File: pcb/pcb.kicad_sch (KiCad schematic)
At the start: 44 parts, among them J1 Conn_01x02_Socket, J2 Conn_01x04_Socket, U1 AP2112K-3.3TRG1, U2 W25Q16JVUXIQ, U3 RP2040, U4 DS4432U+T&amp;R, U5 AD8403ARUZ1-REEL, U6 ADG801BRTZ-REEL7, Y2 Crystal_GND24_Small

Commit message: Order ready
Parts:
- C10, C11, C12, C13, C14, C15, C16, C18, C19, C3, C8, C9: LCSC C394158 -> (none)
- C4, C5: value 15p -> 10p
- C6, C7: LCSC C412453 -> (none)
- D1, D2: LCSC C2971749 -> C99683
- R1, R2: LCSC C138073 -> (none)
- R11: value 91 -> 24; LCSC C2974023 -> (none)
- R3, R4: LCSC C705665 -> (none)
- R5, R6: LCSC C102938 -> (none)
- R7, R8: LCSC C144716 -> (none)
- R9: LCSC C3152120 -> (none)
- Y2: LCSC (none) -> C9002
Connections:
- net +3V3: now also U3.26 (RUN)
- no-connect marks 14 -> 13
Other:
- note added: "IF=20[mA] VF=2.7-3.0[V], Estimated typical=2.85[V] (3.3 - 2.85) / 0.02 = 22.5[Ω] 24Ω seems to be the easy to purchase."
- note added: "Must be approximately 90[Ω] according to USB specifications. 1[mm] board, 0.25[mm] spacing, then 0.9[mm] wiring width."
- note added: "This capacitor is shared between pins 48 and 49."
- note added: "VBUS and 3DS 5V should be wired as thick as possible."
- note added: "cf. Raspberry Pi Pico AEL X12M000000S096 Frequency=12MHz ESR=50[Ω] Load Capacitance=10[pF] Tolerance=±30[ppm] Estimated stray capacity=5[pF] Using ESR=80[Ω], load capacitance=10[pF] at this time. 10 = (C4 * C5) / (C4 + C5) + 5 C4 = C5 = 10[pF]"
- note added: "cf. https://www.raspberrypi.com/documentation/microcontrollers/debug-probe.html#schematics"
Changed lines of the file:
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@@
 (kicad_sch (version 20230121) (generator eeschema)
   (paper "A4")
+  (junction (at 209.55 48.26) (diameter 0) (color 0 0 0 0)
+  )
   (junction (at 72.39 63.5) (diameter 0) (color 0 0 0 0)
   )
@@
   (no_connect (at 22.86 40.64))
   (no_connect (at 68.58 184.15))
-  (no_connect (at 173.99 119.38))
   (wire (pts (xy 214.63 45.72) (xy 256.54 45.72))
     (stroke (width 0) (type default))
@@
     (stroke (width 0) (type default))
   )
+  (wire (pts (xy 173.99 119.38) (xy 209.55 119.38))
+    (stroke (width 0) (type default))
+  )
   (wire (pts (xy 22.86 13.97) (xy 22.86 22.86))
     (stroke (width 0) (type default))
@@
     (stroke (width 0) (type default))
   )
+  (wire (pts (xy 209.55 119.38) (xy 209.55 48.26))
+    (stroke (width 0) (type default))
+  )
   (wire (pts (xy 245.11 55.88) (xy 237.49 55.88))
     (stroke (width 0) (type default))
@@
     (effects (font (size 1.27 1.27)) (justify left bottom))
   )
+  (text "Must be approximately 90[Ω] according to USB specifications.\n1[mm] board, 0.25[mm] spacing, then 0.9[mm] wiring width."
+    (at 260.35 55.88 0)
+    (effects (font (size 1.27 1.27)) (justify left bottom))
+  )
+  (text "cf. Raspberry Pi Pico\nAEL X12M000000S096\nFrequency=12MHz\nESR=50[Ω]\nLoad Capacitance=10[pF]\nTolerance=±30[ppm]\n\nEstimated stray capacity=5[pF]\n\nUsing ESR=80[Ω], load capacitance=10[pF] at this time.\n\n10 = (C4 * C5) / (C4 + C5) + 5\nC4 = C5 = 10[pF]\n"
+    (at 15.24 125.73 0)
+    (effects (font (size 1.27 1.27)) (justify left bottom))
+  )
+  (text "cf. https://www.raspberrypi.com/documentation/microcontrollers/debug-probe.html#schematics"
+    (at 95.25 16.51 0)
+    (effects (font (size 1.27 1.27)) (justify left bottom))
+  )
+  (text "IF=20[mA]\nVF=2.7-3.0[V], Estimated typical=2.85[V]\n(3.3 - 2.85) / 0.02 = 22.5[Ω]\n\n24Ω seems to be the easy to purchase."
+    (at 250.19 143.51 0)
+    (effects (font (size 1.27 1.27)) (justify left bottom))
+  )
+  (text "VBUS and 3DS 5V should be wired as thick as possible."
+    (at 76.2 44.45 0)
+    (effects (font (size 1.27 1.27)) (justify left bottom))
+  )
+  (text "This capacitor is shared between pins 48 and 49." (at 207.01 29.21 0)
+    (effects (font (size 1.27 1.27)) (justify left bottom))
+  )
   (label "USB_D-" (at 237.49 58.42 0) (fields_autoplaced)
     (effects (font (size 1.27 1.27)) (justify left bottom))
@@
       (effects (font (size 1.27 1.27)) hide)
     )
-    (property "LCSC" "C394158" (at 180.34 34.29 0)
-      (effects (font (size 1.27 1.27)) hide)
-    )
     (pin "1")
     (pin "2")
@@
       (effects (font (size 1.27 1.27)) hide)
     )
+    (property "LCSC" "C9002" (at 33.02 86.36 0)
+      (effects (font (size 1.27 1.27)) hide)
+    )
     (pin "1")
     (pin "2")
@@
       (effects (font (size 1.27 1.27)) hide)
     )
-    (property "LCSC" "C394158" (at 208.28 34.29 0)
-      (effects (font (size 1.27 1.27)) hide)
-    )
     (pin "1")
     (pin "2")
@@
       (effects (font (size 1.27 1.27)) hide)
     )
-    (property "LCSC" "C144716" (at 82.55 104.14 90)
-      (effects (font (size 1.27 1.27)) hide)
-    )
     (pin "1")
     (pin "2")
@@
       (effects (font (size 1.27 1.27)) hide)
     )
-    (property "LCSC" "C138073" (at 20.32 33.02 90)
-      (effects (font (size 1.27 1.27)) hide)
-    )
     (pin "1")
     (pin "2")
@@
       (effects (font (size 1.27 1.27)) hide)
     )
-    (property "LCSC" "C705665" (at 72.39 58.42 0)
-      (effects (font (size 1.27 1.27)) hide)
-    )
     (pin "1")
     (pin "2")
@@
       (effects (font (size 1.27 1.27)) hide)
     )
-    (property "LCSC" "C394158" (at 259.08 34.29 0)
-      (effects (font (size 1.27 1.27)) hide)
-    )
     (pin "1")
     (pin "2")
@@
       (effects (font (size 1.27 1.27)) hide)
     )
-    (property "LCSC" "C2971749" (at 85.09 22.86 0)
+    (property "LCSC" "C99683" (at 85.09 22.86 0)
       (effects (font (size 1.27 1.27)) hide)
     )
@@
       (effects (font (size 1.27 1.27)) hide)
     )
-    (property "LCSC" "C394158" (at 238.76 34.29 0)
-      (effects (font (size 1.27 1.27)) hide)
-    )
     (pin "1")
     (pin "2")
@@
       (effects (font (size 1.27 1.27)) hide)
     )
-    (property "LCSC" "C412453" (at 199.39 34.29 0)
-      (effects (font (size 1.27 1.27)) hide)
-    )
     (pin "1")
     (pin "2")
@@
       (effects (font (size 1.27 1.27)) hide)
     )
-    (property "LCSC" "C2971749" (at 85.09 27.94 0)
+    (property "LCSC" "C99683" (at 85.09 27.94 0)
       (effects (font (size 1.27 1.27)) hide)
     )
@@
       (effects (font (size 1.27 1.27)) hide)
     )
-    (property "LCSC" "C138073" (at 48.26 40.64 90)
-      (effects (font (size 1.27 1.27)) hide)
-    )
     (pin "1")
     (pin "2")
@@
       (effects (font (size 1.27 1.27)) hide)
     )
-    (property "LCSC" "C3152120" (at 92.71 144.78 90)
-      (effects (font (size 1.27 1.27)) hide)
-    )
     (pin "1")
     (pin "2")
@@
       (effects (font (size 1.27 1.27)) hide)
     )
-    (property "LCSC" "C412453" (at 189.23 34.29 0)
-      (effects (font (size 1.27 1.27)) hide)
-    )
     (pin "1")
     (pin "2")
@@
       (effects (font (size 1.27 1.27)) hide)
     )
-    (property "LCSC" "C705665" (at 57.15 83.82 0)
-      (effects (font (size 1.27 1.27)) hide)
-    )
     (pin "1")
     (pin "2")
@@
       (effects (font (size 1.27 1.27)) hide)
     )
-    (property "LCSC" "C144716" (at 110.49 106.68 90)
-      (effects (font (size 1.27 1.27)) hide)
-    )
     (pin "1")
     (pin "2")
@@
       (effects (font (size 1.27 1.27)) hide)
     )
-    (property "LCSC" "C102938" (at 248.92 55.88 90)
-      (effects (font (size 1.27 1.27)) hide)
-    )
     (pin "1")
     (pin "2")
@@
       (effects (font (size 1.27 1.27)) (justify left))
     )
-    (property "Value" "15p" (at 59.69 90.8113 0)
+    (property "Value" "10p" (at 59.69 90.8113 0)
       (effects (font (size 1.27 1.27)) (justify left))
     )
@@
       (effects (font (size 1.27 1.27)) hide)
     )
-    (property "LCSC" "C394158" (at 29.21 191.77 0)
-      (effects (font (size 1.27 1.27)) hide)
-    )
     (pin "1")
     (pin "2")
@@
       (effects (font (size 1.27 1.27)))
     )
-    (property "Value" "91" (at 251.46 129.54 90)
+    (property "Value" "24" (at 251.46 129.54 90)
       (effects (font (size 1.27 1.27)))
     )
@@
       (effects (font (size 1.27 1.27)) hide)
     )
-    (property "LCSC" "C2974023" (at 251.46 127 90)
-      (effects (font (size 1.27 1.27)) hide)
-    )
     (pin "1")
     (pin "2")
@@
       (effects (font (size 1.27 1.27)) (justify left))
     )
-    (property "Value" "15p" (at 22.86 90.8113 0)
+    (property "Value" "10p" (at 22.86 90.8113 0)
       (effects (font (size 1.27 1.27)) (justify left))
     )
@@
       (effects (font (size 1.27 1.27)) hide)
     )
-    (property "LCSC" "C394158" (at 248.92 34.29 0)
-      (effects (font (size 1.27 1.27)) hide)
-    )
     (pin "1")
     (pin "2")
@@
       (effects (font (size 1.27 1.27)) hide)
     )
-    (property "LCSC" "C102938" (at 248.92 58.42 90)
-      (effects (font (size 1.27 1.27)) hide)
-    )
     (pin "1")
     (pin "2")
@@
       (effects (font (size 1.27 1.27)) hide)
     )
-    (property "LCSC" "C394158" (at 228.6 34.29 0)
-      (effects (font (size 1.27 1.27)) hide)
-    )
     (pin "1")
     (pin "2")
@@
       (effects (font (size 1.27 1.27)) hide)
     )
-    (property "LCSC" "C394158" (at 170.18 34.29 0)
-      (effects (font (size 1.27 1.27)) hide)
-    )
     (pin "1")
     (pin "2")
@@
       (effects (font (size 1.27 1.27)) hide)
     )
-    (property "LCSC" "C394158" (at 218.44 34.29 0)
-      (effects (font (size 1.27 1.27)) hide)
-    )
     (pin "1")
     (pin "2")
@@
       (effects (font (size 1.27 1.27)) hide)
     )
-    (property "LCSC" "C394158" (at 86.36 160.02 0)
-      (effects (font (size 1.27 1.27)) hide)
-    )
     (pin "1")
     (pin "2")
@@
       (effects (font (size 1.27 1.27)) hide)
     )
-    (property "LCSC" "C394158" (at 270.51 34.29 0)
-      (effects (font (size 1.27 1.27)) hide)
-    )
     (pin "1")
     (pin "2")
@@
       (effects (font (size 1.27 1.27)) hide)
     )
-    (property "LCSC" "C394158" (at 146.05 66.04 0)
-      (effects (font (size 1.27 1.27)) hide)
-    )

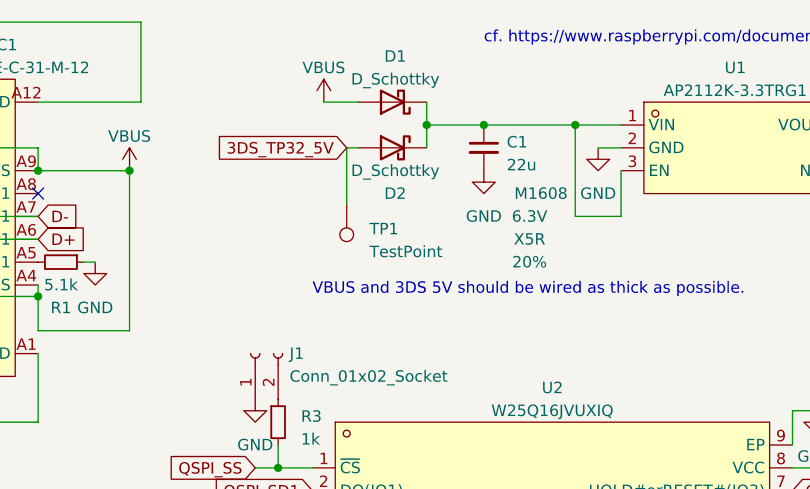
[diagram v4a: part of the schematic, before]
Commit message: Type-C connector stick out as much as possible
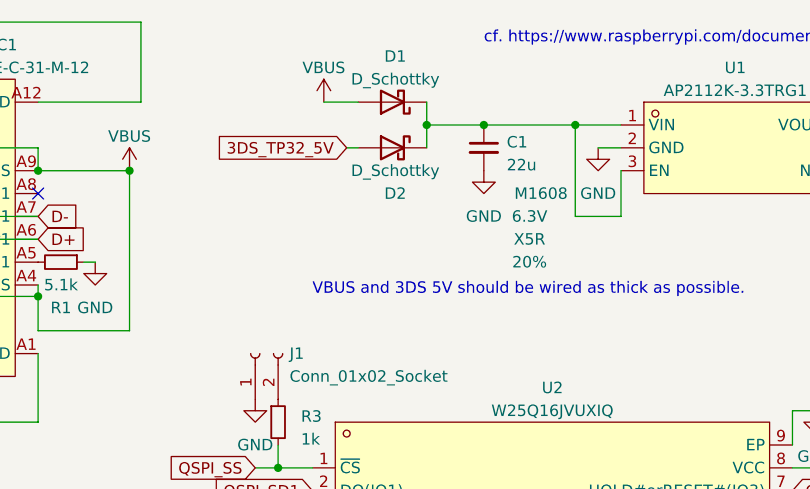
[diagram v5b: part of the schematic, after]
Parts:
- removed TP1: TestPoint, TestPoint:TestPoint_Pad_D1.5mm, symbol Connector:TestPoint
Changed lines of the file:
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@@
-    (stroke (width 0) (type default))
-  )
-  (wire (pts (xy 80.01 34.29) (xy 80.01 27.94))
     (stroke (width 0) (type default))
   )
@@
         )
       )
-    )
-  )
-  (symbol (lib_id "Connector:TestPoint") (at 80.01 34.29 180) (unit 1)
-    (in_bom yes) (on_board yes) (dnp no) (fields_autoplaced)
-    (property "Reference" "TP1" (at 82.55 36.957 0)
-      (effects (font (size 1.27 1.27)) (justify right))
-    )
-    (property "Value" "TestPoint" (at 82.55 39.497 0)
-      (effects (font (size 1.27 1.27)) (justify right))
-    )
-    (property "Footprint" "TestPoint:TestPoint_Pad_D1.5mm" (at 74.93 34.29 0)
-      (effects (font (size 1.27 1.27)) hide)
-    )
-    (property "Datasheet" "~" (at 74.93 34.29 0)
-      (effects (font (size 1.27 1.27)) hide)
-    )
-    (pin "1")
-    (instances
-      (project "pcb"
-        (path "/4db5c0ae-dab5-4243-9886-99aa858b7752"
-          (reference "TP1") (unit 1)
-        )
-      )

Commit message: Update schematic
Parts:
- removed D3: LED_Small, LED_SMD:LED_0402_1005Metric, symbol Device:LED_Small
- removed R11: 24, Resistor_SMD:R_0402_1005Metric, symbol Device:R_Small
- added LED1: SML-LX0404SIUPGUSB, SML-LX0404SIUPGUSB, symbol SML-LX0404SIUPGUSB:SML-LX0404SIUPGUSB
- added R10: 620, Resistor_SMD:R_0402_1005Metric, symbol Device:R
- added R11: 180, Resistor_SMD:R_0402_1005Metric, symbol Device:R
- added R12: 240, Resistor_SMD:R_0402_1005Metric, symbol Device:R
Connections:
- net +3V3: now also LED1.1 (COMMON_ANODE)
- net at U3.35 (GPIO23): now also R10.1
- net at U3.36 (GPIO24): now also R11.2
- net at U3.37 (GPIO25): now also R12.2
- new net: LED1.2 (CATHODE_RED), R10.2
- new net: LED1.3 (CATHODE_BLUE), R12.1
- new net: LED1.4 (CATHODE_GREEN), R11.1
- no-connect marks 13 -> 11
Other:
- note added: "Use E24 Resistors R: (3.3 - 2.15) / 0.002 ≈ 620[Ω] G: (3.3 - 2.95) / 0.002 ≈ 180[Ω] B: (3.3 - 2.85) / 0.002 ≈ 240[Ω]"
- note removed: "IF=20[mA] VF=2.7-3.0[V], Estimated typical=2.85[V] (3.3 - 2.85) / 0.02 = 22.5[Ω] 24Ω seems to be the easy to purchase."

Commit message: Update PCB
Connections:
- net 3DS_TP68_V: now also U4.6 (OUT0); no longer U4.7 (OUT1)
- net 3DS_TP69_H: now also U4.7 (OUT1); no longer U4.6 (OUT0)

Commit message: Resize
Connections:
- net +3V3: no longer LED1.1 (COMMON_ANODE)
- net LED_ANODE: now reaches U3.35 (GPIO23)
- net LED_ANODE: now also LED1.1 (COMMON_ANODE); no longer R10.1
- net LED_GREEN: now reaches R11.2
- net LED_GREEN: now also U3.37 (GPIO25); no longer U3.36 (GPIO24)
- net LED_BLUE: now reaches R12.2
- net LED_BLUE: now also U3.40 (GPIO28_ADC2); no longer U3.37 (GPIO25)
- net RELAY_A renamed SW_IN
- new net LED_RED: R10.1, U3.36 (GPIO24)
- no-connect marks 11 -> 10
